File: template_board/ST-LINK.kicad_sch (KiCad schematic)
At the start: 38 parts, among them Q2 MMST3904, U7 STM32F103CBTx, Y5 8 MHz

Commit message: update pcb leyout goruping
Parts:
- removed TP10, TP11, TP12, TP8, TP9: ~, TestPoint:TestPoint_Pad_D1.0mm, symbol Connector:TestPoint
- added J4: SWD, Connector_PinSocket_2.54mm:PinSocket_1x05_P2.54mm_Vertical, symbol Connector_Generic:Conn_01x05

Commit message: schemat skończony
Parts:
- removed TP6, TP7: TestPoint, TestPoint:TestPoint_Pad_D1.0mm, symbol Connector:TestPoint
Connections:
- net STLINK_RX renamed STLINK_UART.RX
- net STLINK_TX renamed STLINK_UART.TX

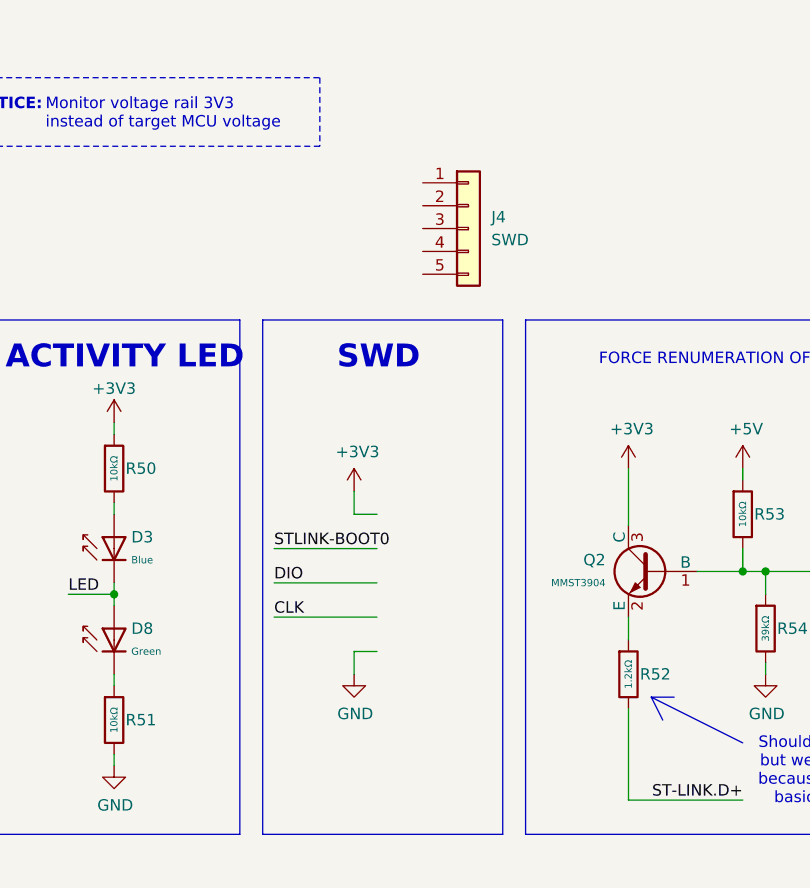
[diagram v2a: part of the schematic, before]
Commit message: sub leyoyut partially completed
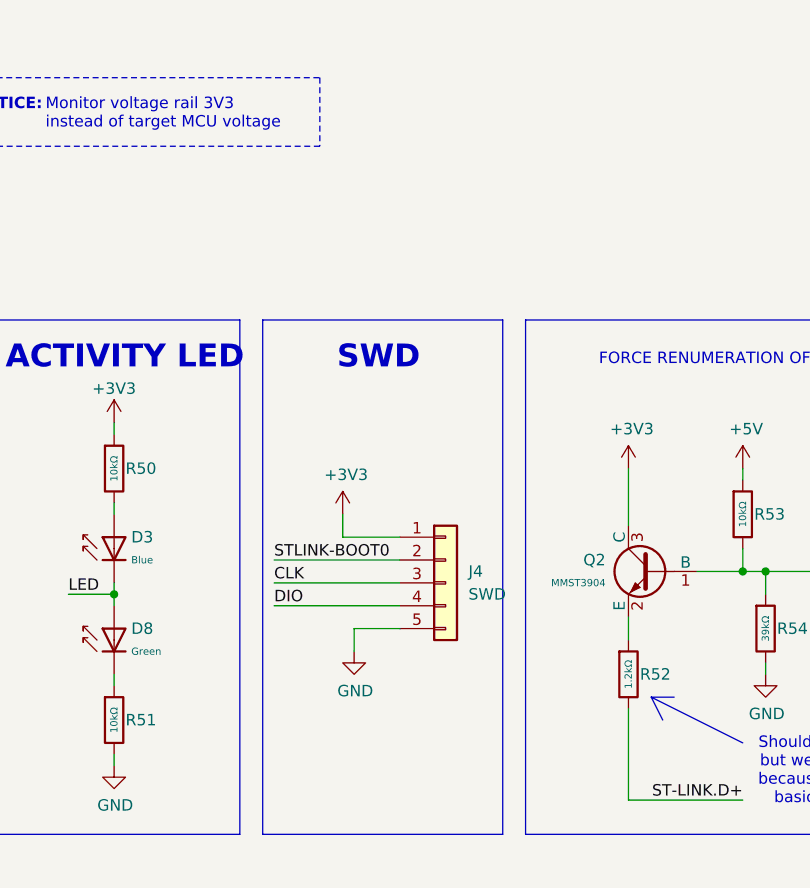
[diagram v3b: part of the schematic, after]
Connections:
- net +3V3: now also J4.1 (Pin_1)
- net CLK: now also J4.3 (Pin_3)
- net DIO: now also J4.4 (Pin_4)
- net GND: now also J4.5 (Pin_5)
- net STLINK-BOOT0: now also J4.2 (Pin_2)
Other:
- moved on the sheet: J4
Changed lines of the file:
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@@
 		(rev "1.0")
 		(company "Patryk Dudziński")
-		(comment 1 "Referenced on desing from Artem Horiunov, Dominik Pluta")
 	)
 	(junction
@@
 	(wire
 		(pts
-			(xy 193.04 91.44) (xy 204.47 91.44)
+			(xy 193.04 92.71) (xy 207.01 92.71)
 		)
 		(stroke
@@
 	(wire
 		(pts
-			(xy 193.04 95.25) (xy 204.47 95.25)
+			(xy 58.42 85.09) (xy 72.39 85.09)
 		)
 		(stroke
@@
 	(wire
 		(pts
-			(xy 58.42 85.09) (xy 72.39 85.09)
+			(xy 38.1 78.74) (xy 38.1 85.09)
 		)
 		(stroke
@@
 	(wire
 		(pts
-			(xy 38.1 78.74) (xy 38.1 85.09)
+			(xy 110.49 158.75) (xy 125.73 158.75)
 		)
 		(stroke
@@
 	(wire
 		(pts
-			(xy 110.49 158.75) (xy 125.73 158.75)
+			(xy 129.54 95.25) (xy 116.84 95.25)
 		)
 		(stroke
@@
 	(wire
 		(pts
-			(xy 129.54 95.25) (xy 116.84 95.25)
+			(xy 201.93 100.33) (xy 201.93 102.87)
 		)
 		(stroke
@@
 	(wire
 		(pts
+			(xy 193.04 97.79) (xy 207.01 97.79)
+		)
+		(stroke
+			(width 0)
+			(type default)
+		)
+	)
+	(wire
+		(pts
 			(xy 71.12 38.1) (xy 71.12 39.37)
 		)
@@
 		)
 	)
-	(wire
-		(pts
-			(xy 201.93 102.87) (xy 201.93 105.41)
-		)
-		(stroke
-			(width 0)
-			(type default)
-		)
-	)
 	(polyline
 		(pts
@@
 	(wire
 		(pts
+			(xy 193.04 95.25) (xy 207.01 95.25)
+		)
+		(stroke
+			(width 0)
+			(type default)
+		)
+	)
+	(wire
+		(pts
 			(xy 110.49 170.18) (xy 124.46 170.18)
 		)
@@
 	(wire
 		(pts
-			(xy 204.47 102.87) (xy 201.93 102.87)
+			(xy 53.34 46.99) (xy 53.34 48.26)
 		)
 		(stroke
@@
 	(wire
 		(pts
-			(xy 53.34 46.99) (xy 53.34 48.26)
+			(xy 62.23 38.1) (xy 71.12 38.1)
 		)
 		(stroke
@@
 	(wire
 		(pts
-			(xy 62.23 38.1) (xy 71.12 38.1)
+			(xy 110.49 175.26) (xy 124.46 175.26)
 		)
 		(stroke
@@
 	(wire
 		(pts
-			(xy 110.49 175.26) (xy 124.46 175.26)
+			(xy 247.65 104.14) (xy 247.65 105.41)
 		)
 		(stroke
@@
 	(wire
 		(pts
-			(xy 247.65 104.14) (xy 247.65 105.41)
+			(xy 44.45 46.99) (xy 44.45 48.26)
 		)
 		(stroke
@@
 	(wire
 		(pts
-			(xy 44.45 46.99) (xy 44.45 48.26)
+			(xy 66.04 62.23) (xy 83.82 62.23)
 		)
 		(stroke
@@
 	(wire
 		(pts
-			(xy 66.04 62.23) (xy 83.82 62.23)
+			(xy 78.74 115.57) (xy 83.82 115.57)
 		)
 		(stroke
@@
 	(wire
 		(pts
-			(xy 78.74 115.57) (xy 83.82 115.57)
+			(xy 201.93 100.33) (xy 207.01 100.33)
 		)
 		(stroke
@@
 	(wire
 		(pts
-			(xy 201.93 87.63) (xy 204.47 87.63)
+			(xy 200.66 90.17) (xy 207.01 90.17)
 		)
 		(stroke
@@
 	(wire
 		(pts
-			(xy 201.93 85.09) (xy 201.93 87.63)
+			(xy 200.66 87.63) (xy 200.66 90.17)
 		)
 		(stroke
@@
 	(wire
 		(pts
-			(xy 193.04 99.06) (xy 204.47 99.06)
-		)
-		(stroke
-			(width 0)
-			(type default)
-		)
-	)
-	(wire
-		(pts
 			(xy 38.1 67.31) (xy 38.1 78.74)
 		)
@@
 	)
 	(label "STLINK-BOOT0"
-		(at 193.04 91.44 0)
+		(at 193.04 92.71 0)
 		(effects
 			(font
@@
 		)
 	)
-	(label "DIO"
+	(label "CLK"
 		(at 193.04 95.25 0)
 		(effects
@@
 		)
 	)
+	(label "DIO"
+		(at 193.04 97.79 0)
+		(effects
+			(font
+				(size 1.27 1.27)
+			)
+			(justify left bottom)
+		)
+	)
 	(label "SWD.SWCLK"
 		(at 43.18 118.11 0)
@@
 		)
 	)
-	(label "CLK"
-		(at 193.04 99.06 0)
-		(effects
-			(font
-				(size 1.27 1.27)
-			)
-			(justify left bottom)
-		)
-	)
 	(label "SWD.~{RST}"
 		(at 110.49 175.26 0)
@@
 	(symbol
 		(lib_id "Connector_Generic:Conn_01x05")
-		(at 214.63 55.88 0)
+		(at 212.09 95.25 0)
 		(unit 1)
 		(exclude_from_sim no)
@@
 		(fields_autoplaced yes)
 		(property "Reference" "J4"
-			(at 217.17 54.6099 0)
+			(at 214.63 93.9799 0)
 			(effects
 				(font
@@
 		)
 		(property "Value" "SWD"
-			(at 217.17 57.1499 0)
+			(at 214.63 96.5199 0)
 			(effects
 				(font
@@
 		)
 		(property "Footprint" "Connector_PinSocket_2.54mm:PinSocket_1x05_P2.54mm_Vertical"
-			(at 214.63 55.88 0)
+			(at 212.09 95.25 0)
 			(effects
 				(font
@@
 		)
 		(property "Datasheet" "~"
-			(at 214.63 55.88 0)
+			(at 212.09 95.25 0)
 			(effects
 				(font
@@
 		)
 		(property "Description" "Generic connector, single row, 01x05, script generated (kicad-library-utils/schlib/autogen/connector/)"
-			(at 214.63 55.88 0)
+			(at 212.09 95.25 0)
 			(effects
 				(font
@@
 	(symbol
 		(lib_id "power:+3V3")
-		(at 201.93 85.09 0)
+		(at 200.66 87.63 0)
 		(unit 1)
 		(exclude_from_sim no)
@@
 		(dnp no)
 		(property "Reference" "#PWR056"
-			(at 201.93 88.9 0)
+			(at 200.66 91.44 0)
 			(effects
 				(font
@@
 		)
 		(property "Value" "+3V3"
-			(at 202.311 80.6958 0)
+			(at 201.041 83.2358 0)
 			(effects
 				(font
@@
 		)
 		(property "Footprint" ""
-			(at 201.93 85.09 0)
+			(at 200.66 87.63 0)
 			(effects
 				(font
@@
 		)
 		(property "Datasheet" ""
-			(at 201.93 85.09 0)
+			(at 200.66 87.63 0)
 			(effects
 				(font
@@
 		)
 		(property "Description" ""
-			(at 201.93 85.09 0)
+			(at 200.66 87.63 0)
 			(effects
 				(font
@@
 	(symbol
 		(lib_id "power:GND")
-		(at 201.93 105.41 0)
+		(at 201.93 102.87 0)
 		(unit 1)
 		(exclude_from_sim no)
@@
 		(dnp no)
 		(property "Reference" "#PWR057"
-			(at 201.93 111.76 0)
+			(at 201.93 109.22 0)
 			(effects
 				(font
@@
 		)
 		(property "Value" "GND"
-			(at 202.057 109.8042 0)
+			(at 202.057 107.2642 0)
 			(effects
 				(font
@@
 		)
 		(property "Footprint" ""
-			(at 201.93 105.41 0)
+			(at 201.93 102.87 0)
 			(effects
 				(font
@@
 		)
 		(property "Datasheet" ""
-			(at 201.93 105.41 0)
+			(at 201.93 102.87 0)
 			(effects
 				(font
@@
 		)
 		(property "Description" ""
-			(at 201.93 105.41 0)
+			(at 201.93 102.87 0)
 			(effects
 				(font

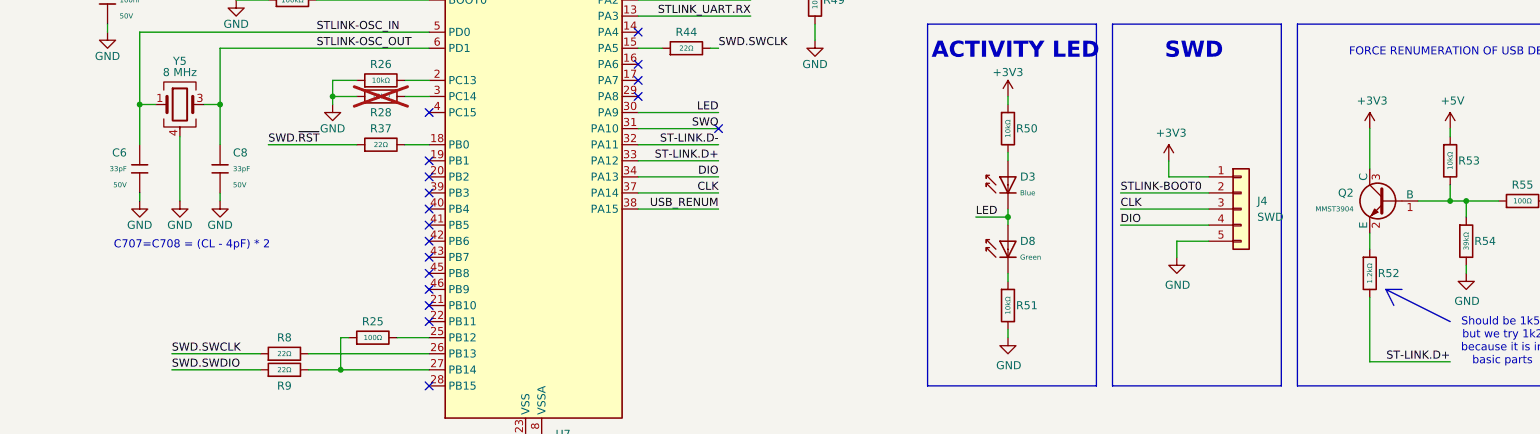
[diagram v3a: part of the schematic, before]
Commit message: [schematics] fixed issue with: stlink->crystal capacitors, usb-> esd with too big capacitance, tranzistor for stlink-usb renum changed
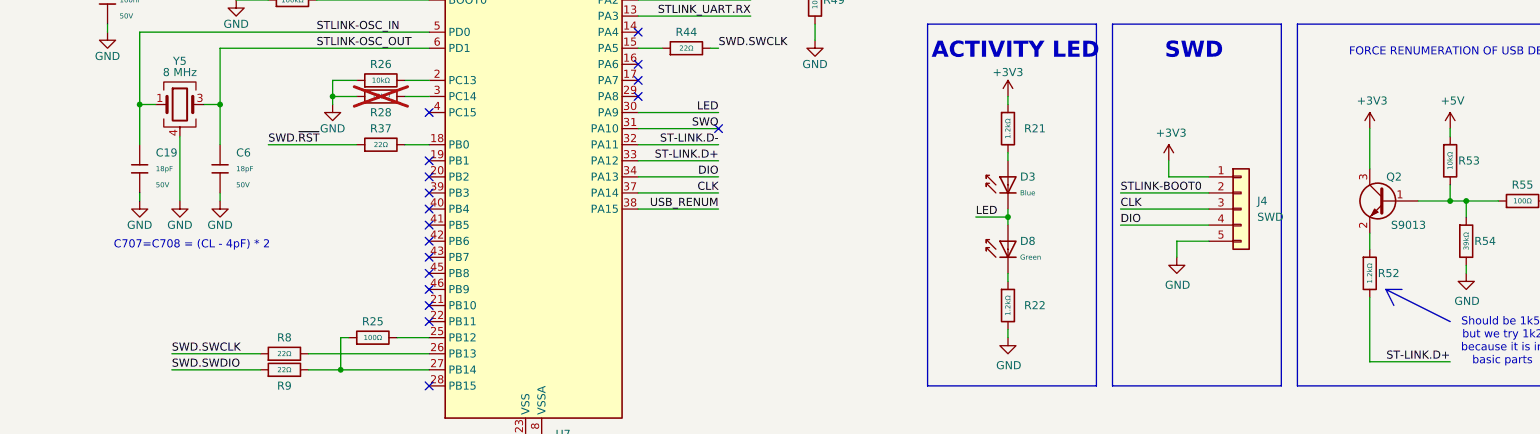
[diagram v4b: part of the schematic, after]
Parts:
- removed C6, C8: 33pF, PCM_JLCPCB:C_0402, symbol PCM_JLCPCB-Capacitors:0402,33pF
- removed Q2: MMST3904, PCM_JLCPCB:Q_SOT-323, symbol PCM_JLCPCB-Transistors:NPN,MMST3904
- removed R50, R51: 10kΩ, PCM_JLCPCB:R_0402, symbol PCM_JLCPCB-Resistors:0402,10kΩ
- added C19, C6: 18pF, PCM_JLCPCB:C_0402, symbol PCM_JLCPCB-Capacitors:0402,18pF
- added Q2: S9013, Package_TO_SOT_SMD:SOT-23, symbol Device:Q_NPN_BEC
- added R21, R22: 1.2kΩ, PCM_JLCPCB:R_0402, symbol PCM_JLCPCB-Resistors:0402,1.2kΩ
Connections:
- net +3V3: now also Q2.3 (C), R21.1
- net GND: now also C19.2, C6.2, R22.2
- net STLINK-OSC_IN: now also C19.1
- net STLINK-OSC_OUT: now also C6.1
- net at R53.2, R54.1, R55.1: now also Q2.1 (B)
- net at D8.1: now also R22.1
- net at R52.1: now also Q2.2 (E)
- net at D3.2: now also R21.2

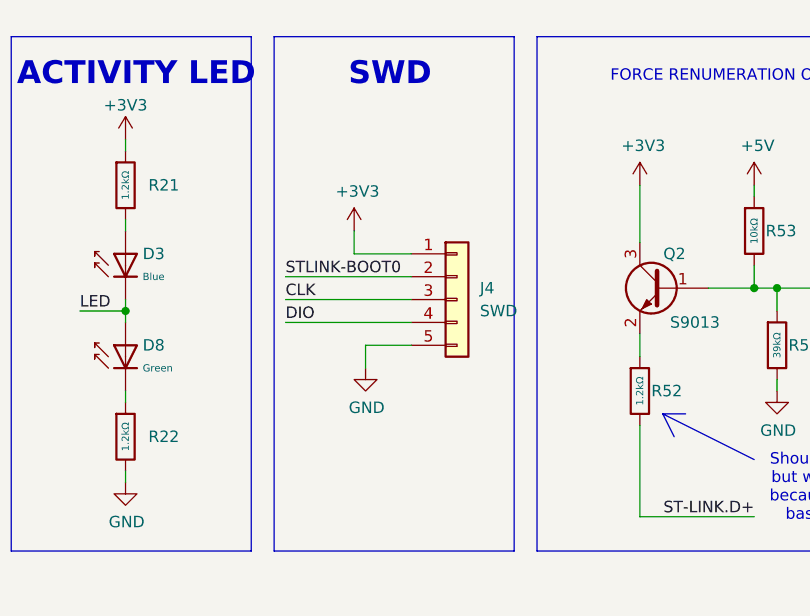
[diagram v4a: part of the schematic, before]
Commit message: [schematics] changed stlink SWD pins
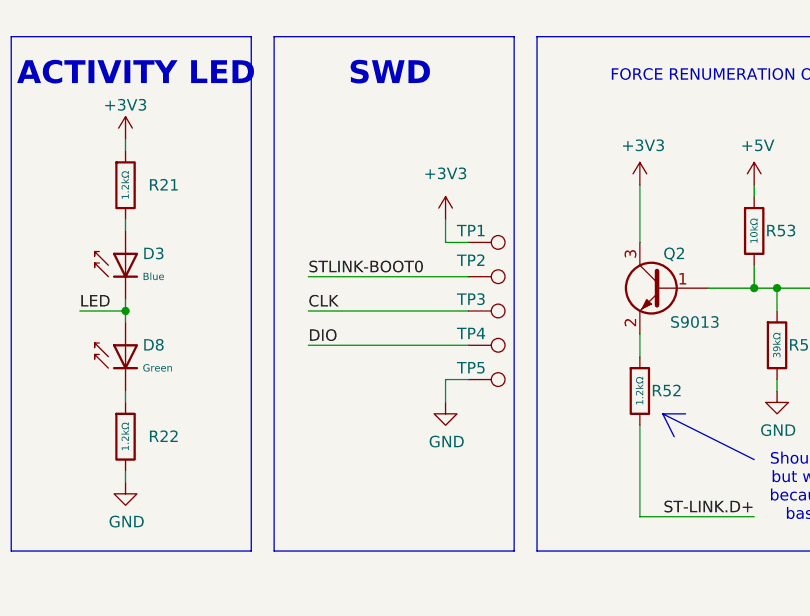
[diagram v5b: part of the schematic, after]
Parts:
- removed J4: SWD, Connector_PinSocket_2.54mm:PinSocket_1x05_P2.54mm_Vertical, symbol Connector_Generic:Conn_01x05
- added TP1, TP2, TP3, TP4, TP5: ~, TestPoint:TestPoint_Pad_D1.0mm, symbol Connector:TestPoint
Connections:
- net +3V3: now also TP1.1
- net CLK: now also TP3.1
- net DIO: now also TP4.1
- net GND: now also TP5.1
- net STLINK-BOOT0: now also TP2.1
